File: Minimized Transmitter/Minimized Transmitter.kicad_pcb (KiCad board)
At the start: 2 copper layers, 27.1 x 27.1 mm, 10 parts, among them J2 Conn_01x02_Male, J4 Conn_01x05_Male, SW1 SW_Push, U1 LPC824M201JHI33, U2 RFM69HCW

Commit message: Done except for deciding on a power switch
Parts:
- added J1: Conn_01x03_Male, my_foot_prints:SlideSwitch_SMD_PN#COM-10860, F.Cu at (141.0, 74.8)
- J2: footprint Connector_PinHeader_2.54mm:PinHeader_1x02_P2.54mm_Vertical -> my_foot_prints:2_pad_sufacemount; moved to B.Cu
- J4: moved to B.Cu
- moved SW1 21.0 mm to (155.9, 69.4), turned to 225 degrees
- moved C1 19.9 mm to (153.7, 71.9), turned to 135 degrees
- moved R2 19.5 mm to (152.7, 72.9), turned to 135 degrees
- moved J4 14.3 mm to (155.5, 70.0), turned to 315 degrees
- moved D1 12.6 mm to (170.0, 70.8), turned to 135 degrees
- moved R1 10.9 mm to (168.0, 68.8), turned to 225 degrees
- moved J2 6.28 mm to (152.0, 76.8), turned to 0 degrees
- moved U1 1.05 mm to (163.3, 69.0)
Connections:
- BT1 pad 1: +3V3 -> Net-(BT1-Pad1)
- U1 pad 10: LED -> Net-(U1-Pad10)
- U1 pad 16: Net-(U1-Pad16) -> LED
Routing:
- net MISO: track 0.00 -> 37.4 mm
- net MOSI: track 0.00 -> 31.8 mm, vias 0 -> 2
- net +3V3: track 0.00 -> 29.5 mm, vias 0 -> 1
- net DIO0: track 0.00 -> 14.0 mm
- net nRESET: track 0.00 -> 13.1 mm, vias 0 -> 1
- net TX: track 0.00 -> 11.9 mm, vias 0 -> 1
- net SCK: track 0.00 -> 8.92 mm
- net NSS: track 0.00 -> 7.51 mm
- net SWDIO: track 0.00 -> 5.50 mm, vias 0 -> 1
- net SWDCLK: track 0.00 -> 4.77 mm, vias 0 -> 1
- net LED: track 0.00 -> 4.45 mm
- net GND: track 0.00 -> 3.81 mm, vias 0 -> 5
- net Net-(D1-Pad2): track 0.00 -> 1.63 mm
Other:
- board text added: "CLK"
- board text added: "IO"
- board text added: "nR"

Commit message: Commit
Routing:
- net GND: track 3.81 -> 14.5 mm
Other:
- board text added: "3v3"
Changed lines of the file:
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@@
-(kicad_pcb (version 20171130) (host pcbnew "(5.0.2)-1")
+(kicad_pcb (version 20171130) (host pcbnew "(5.0.1)-3")
   (general
     (thickness 1.6)
-    (drawings 7)
-    (tracks 101)
+    (drawings 11)
+    (tracks 104)
     (zones 0)
     (modules 11)
@@
     (last_trace_width 0.25)
     (trace_clearance 0.2)
-    (zone_clearance 0.4)
+    (zone_clearance 0.508)
     (zone_45_only no)
     (trace_min 0.2)
@@
       (effects (font (size 0.8 0.8) (thickness 0.12)))
     )
-    (pad 1 smd roundrect (at -1.4 0 135) (size 1.25 1.75) (layers F.Cu F.Paste F.Mask) (roundrect_rratio 0.2)
-      (net 1 GND))
-    (pad 2 smd roundrect (at 1.4 0 135) (size 1.25 1.75) (layers F.Cu F.Paste F.Mask) (roundrect_rratio 0.2)
+    (pad 1 smd roundrect (at -1.399999 0 135) (size 1.25 1.75) (layers F.Cu F.Paste F.Mask) (roundrect_rratio 0.2)
+      (net 1 GND))
+    (pad 2 smd roundrect (at 1.399999 0 135) (size 1.25 1.75) (layers F.Cu F.Paste F.Mask) (roundrect_rratio 0.2)
       (net 36 "Net-(D1-Pad2)"))
     (model ${KISYS3DMOD}/LED_SMD.3dshapes/LED_1206_3216Metric.wrl
@@
     (tags "Surface mounted pin header SMD 2x05 1.27mm double row")
     (attr smd)
-    (fp_text reference J4 (at -1.9 0 225) (layer B.SilkS)
+    (fp_text reference J4 (at 0.141421 -4.525483 225) (layer B.SilkS)
       (effects (font (size 1 1) (thickness 0.15)) (justify mirror))
     )
@@
     (pad 1 smd rect (at 0 2.54 315) (size 2 0.74) (layers B.Cu B.Paste B.Mask)
       (net 2 +3V3))
-    (pad 2 smd rect (at 0 1.27 315) (size 2 0.74) (layers B.Cu B.Paste B.Mask)
+    (pad 2 smd rect (at 0 1.270001 315) (size 2 0.74) (layers B.Cu B.Paste B.Mask)
       (net 1 GND))
     (pad 3 smd rect (at 0 0 315) (size 2 0.74) (layers B.Cu B.Paste B.Mask)
       (net 3 SWDIO))
-    (pad 4 smd rect (at 0 -1.27 315) (size 2 0.74) (layers B.Cu B.Paste B.Mask)
+    (pad 4 smd rect (at 0 -1.270001 315) (size 2 0.74) (layers B.Cu B.Paste B.Mask)
       (net 4 SWDCLK))
     (pad 5 smd rect (at 0 -2.54 315) (size 2 0.74) (layers B.Cu B.Paste B.Mask)
@@
     (tags "Surface mounted pin header SMD 2x05 1.27mm double row")
     (attr smd)
-    (fp_text reference J2 (at -1.9 0 270) (layer B.SilkS)
+    (fp_text reference J2 (at -1.9 0 -90) (layer B.SilkS) hide
       (effects (font (size 1 1) (thickness 0.15)) (justify mirror))
     )
@@
     (pad "" smd rect (at 3.65 1.1 270) (size 1 0.8) (layers F.Cu F.Paste F.Mask))
   )
-  (gr_text IO (at 154.3 68.7) (layer B.SilkS)
+  (gr_text "GND\n" (at 152 78.5) (layer B.SilkS)
+    (effects (font (size 0.6 0.6) (thickness 0.15)) (justify mirror))
+  )
+  (gr_text TX (at 152 75.15) (layer B.SilkS)
+    (effects (font (size 0.6 0.6) (thickness 0.15)) (justify mirror))
+  )
+  (gr_text 3v3 (at 152.75 70.35) (layer B.SilkS)
     (effects (font (size 0.5 0.5) (thickness 0.125)) (justify mirror))
   )
-  (gr_text CLK (at 155.1 67.7) (layer B.SilkS)
+  (gr_text "GND\n" (at 153.6 69.3) (layer B.SilkS)
     (effects (font (size 0.5 0.5) (thickness 0.125)) (justify mirror))
   )
-  (gr_text nR (at 156.1 64.3) (layer B.SilkS)
+  (gr_text IO (at 154.6 68.35) (layer B.SilkS)
+    (effects (font (size 0.5 0.5) (thickness 0.125)) (justify mirror))
+  )
+  (gr_text CLK (at 155.4 67.4) (layer B.SilkS)
+    (effects (font (size 0.5 0.5) (thickness 0.125)) (justify mirror))
+  )
+  (gr_text nR (at 156.9 66.55) (layer B.SilkS)
     (effects (font (size 0.5 0.5) (thickness 0.125)) (justify mirror))
   )
@@
   (via (at 174.5 77.25) (size 0.8) (drill 0.4) (layers F.Cu B.Cu) (net 1))
   (via (at 163.2 77.6) (size 0.8) (drill 0.4) (layers F.Cu B.Cu) (net 1))
+  (segment (start 157.464763 71.864763) (end 163.2 77.6) (width 0.25) (layer B.Cu) (net 1))
+  (segment (start 155.425067 71.864763) (end 157.464763 71.864763) (width 0.25) (layer B.Cu) (net 1))
+  (segment (start 155.025068 71.464764) (end 155.425067 71.864763) (width 0.25) (layer B.Cu) (net 1))
   (via (at 152.25 74) (size 0.8) (drill 0.4) (layers F.Cu B.Cu) (net 2))
   (segment (start 153 73.25) (end 152.25 74) (width 0.25) (layer F.Cu) (net 2))
@@
     (connect_pads (clearance 0.4))
     (min_thickness 0.254)
-    (fill (arc_segments 16) (thermal_gap 0.508) (thermal_bridge_width 0.508))
+    (fill yes (arc_segments 16) (thermal_gap 0.508) (thermal_bridge_width 0.508))
     (polygon
       (pts
@@
   )
   (zone (net 1) (net_name GND) (layer B.Cu) (hatch edge 0.508)
-    (connect_pads yes (clearance 0.508))
+    (connect_pads (clearance 0.508))
     (min_thickness 0.254)
-    (fill (arc_segments 16) (thermal_gap 0.508) (thermal_bridge_width 0.508))
+    (fill yes (arc_segments 16) (thermal_gap 0.508) (thermal_bridge_width 0.508))
     (polygon
       (pts

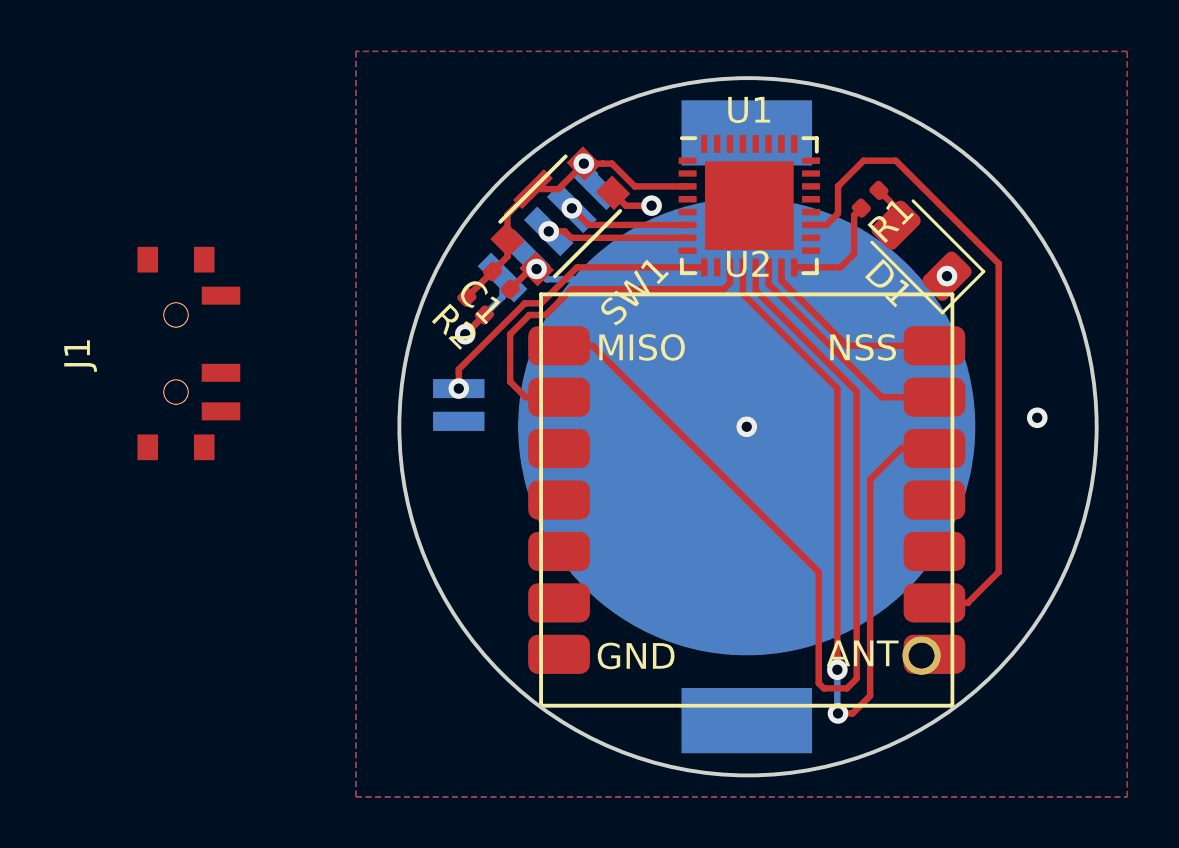
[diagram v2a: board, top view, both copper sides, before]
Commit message: Added switch and finished board
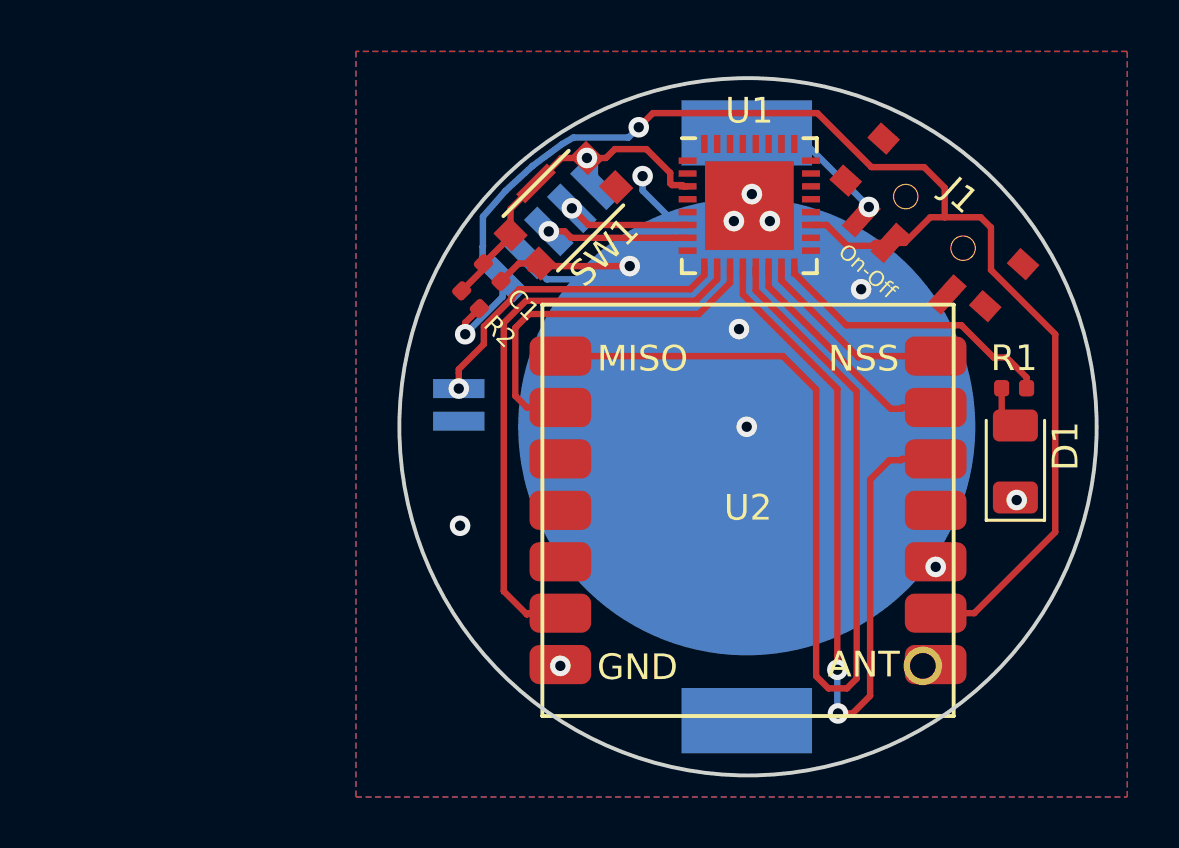
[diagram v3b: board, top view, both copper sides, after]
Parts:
- moved J1 29.9 mm to (170.5, 69.7), turned to 138 degrees
- moved R1 9.24 mm to (173.6, 76.1), turned to 0 degrees
- moved D1 8.98 mm to (173.7, 79.0), turned to 90 degrees
- moved C1 0.47 mm to (153.3, 71.6)
- moved U2 0.40 mm to (163.2, 80.8)
- moved R2 0.32 mm to (152.5, 72.7)
- moved SW1 0.25 mm to (156.1, 69.2)
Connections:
- J1 pad 1: Net-(BT1-Pad1) -> GND
- J1 pad 3: GND -> Net-(BT1-Pad1)
- U1 pad 10: Net-(U1-Pad10) -> Reset
- U2 pad 9: Net-(U2-Pad9) -> Reset
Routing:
- net +3V3: track 29.5 -> 55.4 mm, vias 1 -> 2
- net Reset: track 0.00 -> 22.5 mm
- net GND: track 14.5 -> 28.5 mm, vias 5 -> 12
- net LED: track 4.45 -> 11.4 mm
- net Net-(BT1-Pad1): track 0.00 -> 6.46 mm, vias 0 -> 1
- net MISO: track 37.4 -> 41.2 mm
- net nRESET: track 13.1 -> 14.9 mm
- net TX: track 11.9 -> 12.6 mm
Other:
- board text added: "On-Off"

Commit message: Added ground Via's
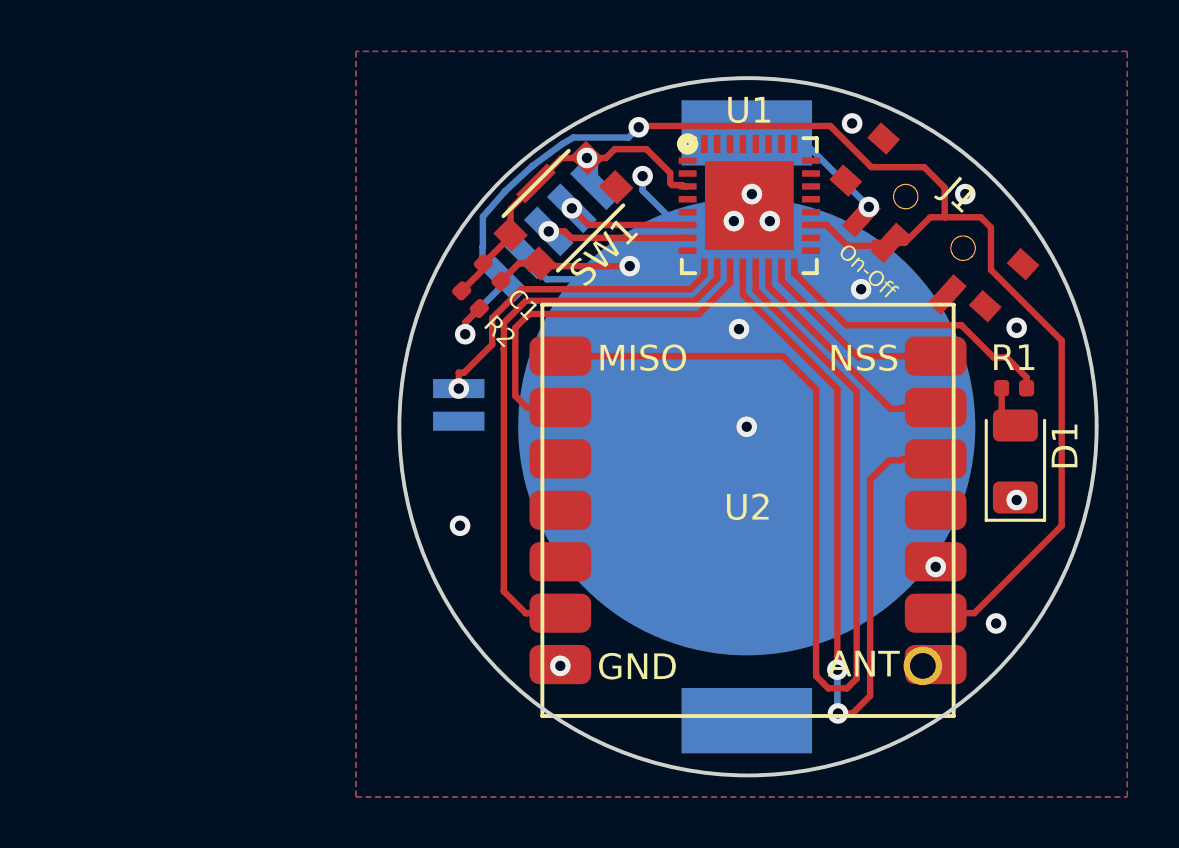
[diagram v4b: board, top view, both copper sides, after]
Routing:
- net GND: vias 12 -> 16
